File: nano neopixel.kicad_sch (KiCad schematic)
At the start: 12 parts

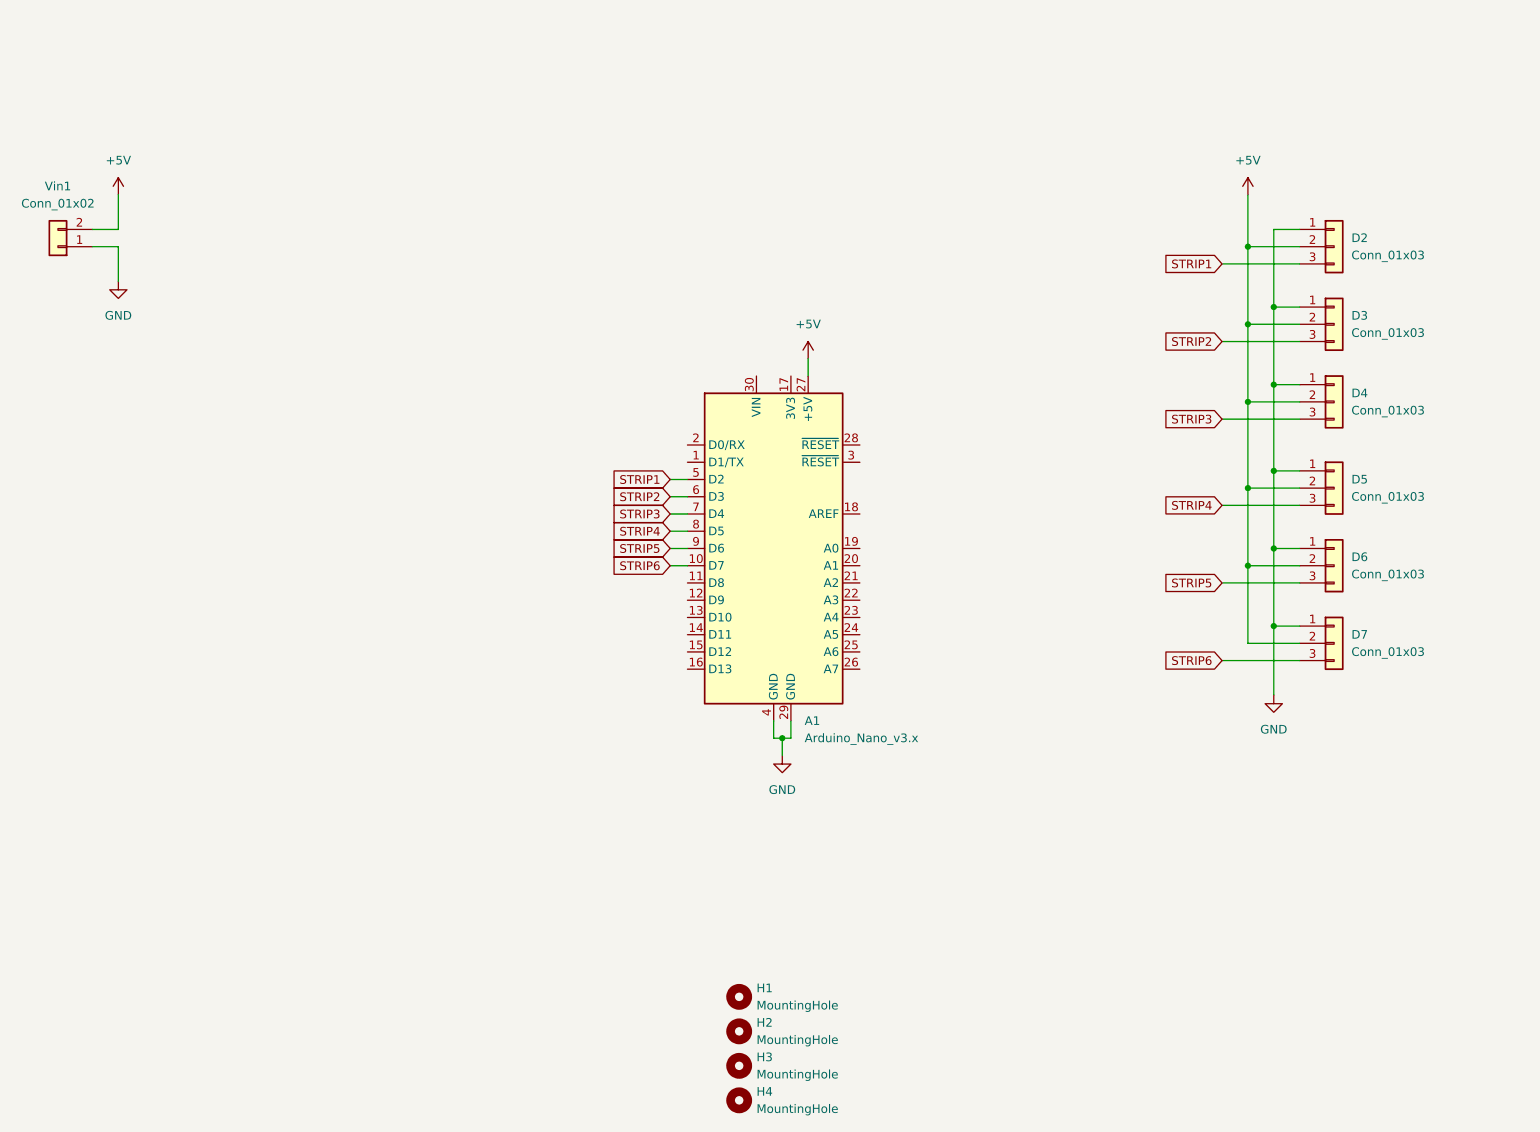
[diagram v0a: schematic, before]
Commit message: added 470ohm signal series resistors, and 1000uF tank cap on Vin
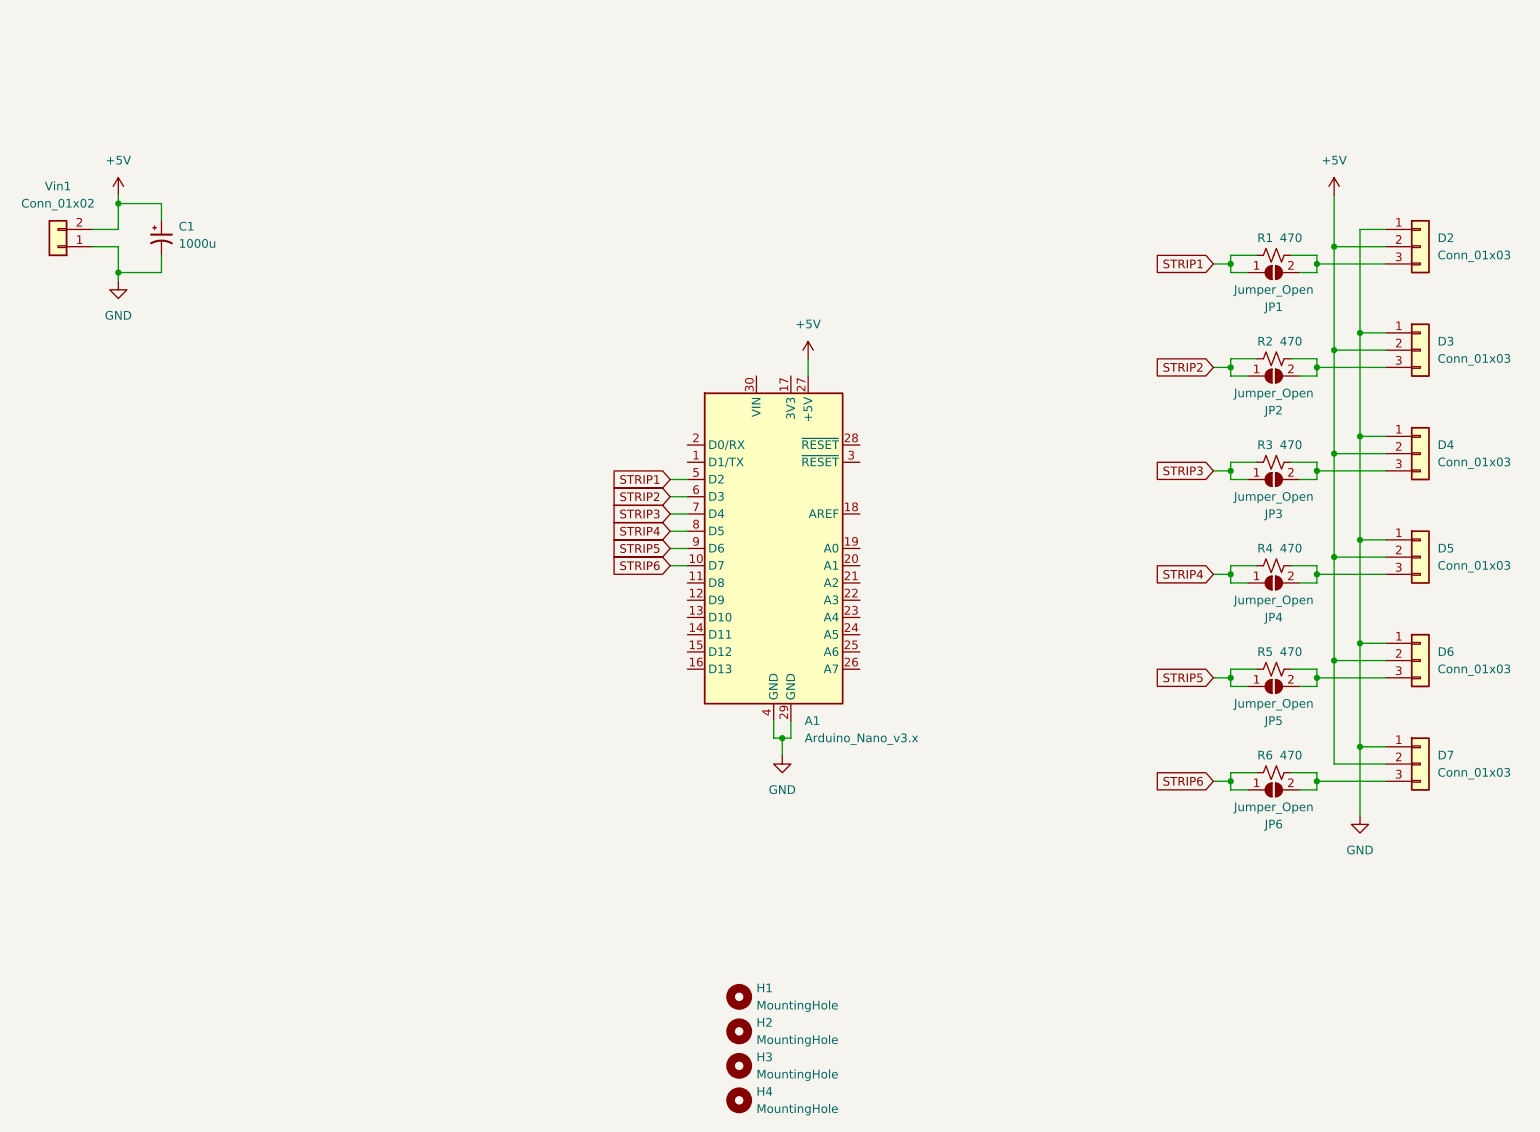
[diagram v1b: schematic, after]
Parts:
- added C1: 1000u, symbol Device:C_Polarized_Small_US
- added JP1, JP2, JP3, JP4, JP5, JP6: Jumper_Open, Jumper:SolderJumper-2_P1.3mm_Open_Pad1.0x1.5mm, symbol Jumper:SolderJumper_2_Open
- added R1, R2, R3, R4, R5, R6: 470, Resistor_SMD:R_0805_2012Metric, symbol Device:R_Small_US
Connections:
- net +5V: now also C1.1
- net GND: now also C1.2
- net STRIP1: now also JP1.1 (A), R1.1; no longer D2.3 (Pin_3)
- net STRIP2: now also JP2.1 (A), R2.1; no longer D3.3 (Pin_3)
- net STRIP3: now also JP3.1 (A), R3.1; no longer D4.3 (Pin_3)
- net STRIP4: now also JP4.1 (A), R4.1; no longer D5.3 (Pin_3)
- net STRIP5: now also JP5.1 (A), R5.1; no longer D6.3 (Pin_3)
- net STRIP6: now also JP6.1 (A), R6.1; no longer D7.3 (Pin_3)
- new net: D3.3 (Pin_3), JP2.2 (B), R2.2
- new net: D6.3 (Pin_3), JP5.2 (B), R5.2
- new net: D5.3 (Pin_3), JP4.2 (B), R4.2
- new net: D2.3 (Pin_3), JP1.2 (B), R1.2
- new net: D7.3 (Pin_3), JP6.2 (B), R6.2
- new net: D4.3 (Pin_3), JP3.2 (B), R3.2
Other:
- moved on the sheet: D2, D3, D4, D5, D6, D7

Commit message: added 2 more DIO connections, routed all traces
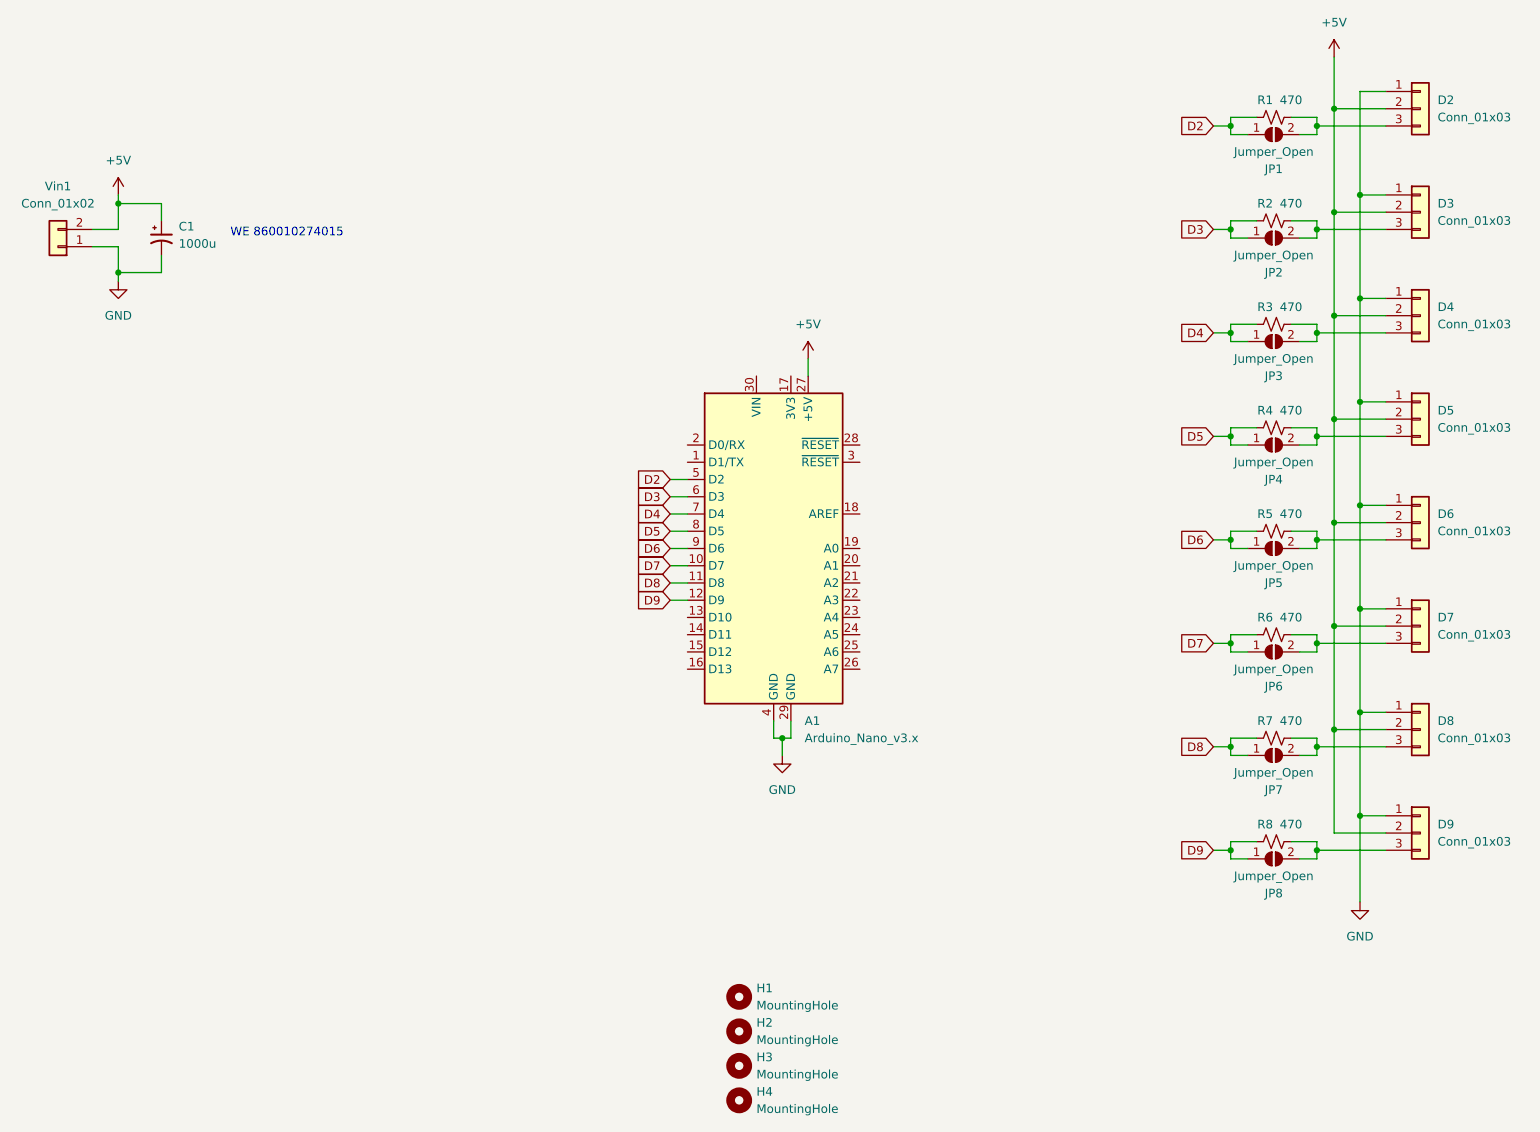
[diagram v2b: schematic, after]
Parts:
- added D8, D9: Conn_01x03, Connector_PinHeader_2.54mm:PinHeader_1x03_P2.54mm_Vertical, symbol Connector_Generic:Conn_01x03
- added JP7, JP8: Jumper_Open, Jumper:SolderJumper-2_P1.3mm_Open_Pad1.0x1.5mm, symbol Jumper:SolderJumper_2_Open
- added R7, R8: 470, Resistor_SMD:R_0805_2012Metric, symbol Device:R_Small_US
- C1: footprint (none) -> Capacitor_THT:CP_Radial_D8.0mm_P3.50mm
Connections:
- net +5V: now also D8.2 (Pin_2), D9.2 (Pin_2)
- net GND: now also D8.1 (Pin_1), D9.1 (Pin_1)
- net D8: now reaches A1.11 (D8)
- net D8: now also JP7.1 (A), R7.1
- net D9: now reaches A1.12 (D9)
- net D9: now also JP8.1 (A), R8.1
- net STRIP1 renamed D2
- net STRIP2 renamed D3
- net STRIP3 renamed D4
- net STRIP4 renamed D5
- net STRIP5 renamed D6
- net STRIP6 renamed D7
- new net: D8.3 (Pin_3), JP7.2 (B), R7.2
- new net: D9.3 (Pin_3), JP8.2 (B), R8.2
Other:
- note added: "WE 860010274015"
- moved on the sheet: D2, D3, D4, D5, D6, D7, JP1, JP2, JP3, JP4, JP5, JP6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

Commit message: added DIO labels to the resistors and jumpers
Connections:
- no-connect marks 0 -> 19
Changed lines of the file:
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@@
   (junction (at 224.79 36.83) (diameter 0) (color 0 0 0 0)
   )
+  (no_connect (at 157.48 99.06))
+  (no_connect (at 157.48 101.6))
+  (no_connect (at 157.48 104.14))
+  (no_connect (at 157.48 106.68))
+  (no_connect (at 157.48 109.22))
+  (no_connect (at 132.08 109.22))
+  (no_connect (at 132.08 111.76))
+  (no_connect (at 132.08 114.3))
+  (no_connect (at 132.08 86.36))
+  (no_connect (at 132.08 83.82))
+  (no_connect (at 142.24 73.66))
+  (no_connect (at 147.32 73.66))
+  (no_connect (at 157.48 83.82))
+  (no_connect (at 157.48 86.36))
+  (no_connect (at 157.48 93.98))
+  (no_connect (at 157.48 111.76))
+  (no_connect (at 157.48 114.3))
+  (no_connect (at 157.48 116.84))
+  (no_connect (at 132.08 116.84))
   (wire (pts (xy 212.09 96.52) (xy 212.09 97.79))
     (stroke (width 0) (type default) (color 0 0 0 0))

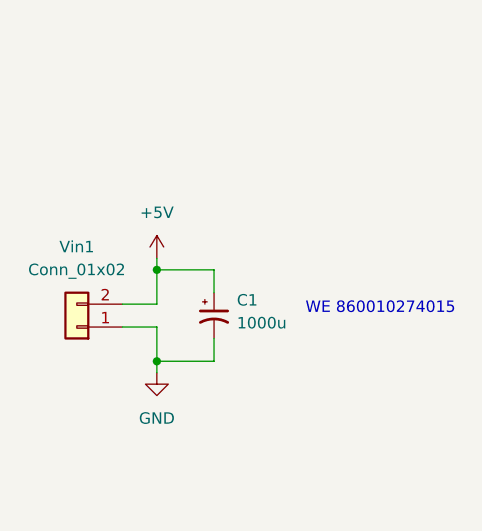
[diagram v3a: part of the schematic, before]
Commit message: Added JLC tracking number location
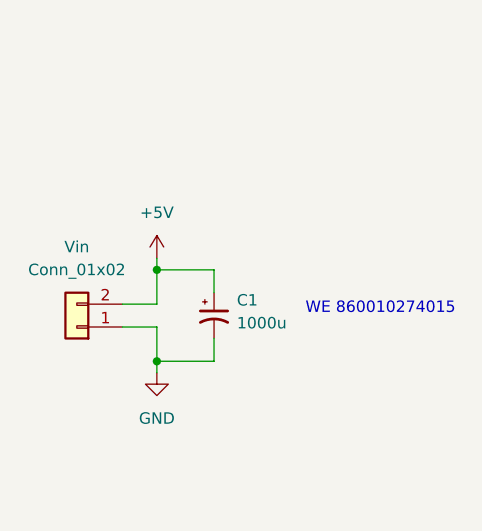
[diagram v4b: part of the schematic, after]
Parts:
- renumbered Vin1 to Vin
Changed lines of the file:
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@@
   (symbol (lib_id "Connector_Generic:Conn_01x02") (at 39.37 54.61 180) (unit 1)
     (in_bom yes) (on_board yes) (fields_autoplaced)
-    (property "Reference" "Vin1" (id 0) (at 39.37 45.72 0))
+    (property "Reference" "Vin" (id 0) (at 39.37 45.72 0))
     (property "Value" "Conn_01x02" (id 1) (at 39.37 48.26 0))
     (property "Footprint" "Connector_PinHeader_2.54mm:PinHeader_1x02_P2.54mm_Vertical" (id 2) (at 39.37 54.61 0)
@@
     )
     (path "/555fd684-9a58-4921-bd99-3bf42d5279c2"
-      (reference "Vin1") (unit 1) (value "Conn_01x02") (footprint "Connector_PinHeader_2.54mm:PinHeader_1x02_P2.54mm_Vertical")
-    )
-  )
+      (reference "Vin") (unit 1) (value "Conn_01x02") (footprint "Connector_PinHeader_2.54mm:PinHeader_1x02_P2.54mm_Vertical")
+    )
+  )

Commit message: added revision
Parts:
- C1: Manufactuter (none) -> Würth Elektronik; mfn (none) -> 860010274015
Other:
- note removed: "WE 860010274015"
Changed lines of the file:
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@@
 (kicad_sch (version 20211123) (generator eeschema)
   (paper "A4")
+  (title_block
+    (date "3/17/2022")
+    (rev "1.1")
+  )
   (junction (at 227.33 80.01) (diameter 0) (color 0 0 0 0)
   )
@@
   (wire (pts (xy 220.98 81.28) (xy 224.79 81.28))
     (stroke (width 0) (type default) (color 0 0 0 0))
-  )
-  (text "WE 860010274015" (at 64.77 53.34 0)
-    (effects (font (size 1.27 1.27)) (justify left bottom))
   )
   (global_label "D2" (shape input) (at 209.55 36.83 180) (fields_autoplaced)
@@
   )
   (symbol (lib_id "Device:C_Polarized_Small_US") (at 54.61 53.34 0) (unit 1)
-    (in_bom yes) (on_board yes) (fields_autoplaced)
+    (in_bom yes) (on_board yes)
     (property "Reference" "C1" (id 0) (at 57.15 51.6381 0)
       (effects (font (size 1.27 1.27)) (justify left))
@@
       (effects (font (size 1.27 1.27)) hide)
     )
-    (property "Datasheet" "~" (id 3) (at 54.61 53.34 0)
-      (effects (font (size 1.27 1.27)) hide)
-    )
-    (pin "1")
+    (property "Datasheet" "https://www.we-online.com/katalog/datasheet/860010274015.pdf" (id 3) (at 54.61 53.34 0)
+      (effects (font (size 1.27 1.27)) hide)
+    )
+    (property "mfn" "860010274015" (id 4) (at 57.15 59.69 0)
+      (effects (font (size 1.27 1.27)) (justify left))
+    )
+    (property "Manufactuter" "Würth Elektronik" (id 5) (at 57.15 57.15 0)
+      (effects (font (size 1.27 1.27)) (justify left))
+    )
+    (pin "1")

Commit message: updated title block with 4488 info
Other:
- company: (none) -> FRC 4488 - SHOCKWAVE
- title: (none) -> NeoPixel driver
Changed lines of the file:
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@@
   (paper "A4")
   (title_block
+    (title "NeoPixel driver")
     (date "3/17/2022")
-    (rev "1.1")
+    (rev "1.0")
+    (company "FRC 4488 - SHOCKWAVE")
   )
   (junction (at 227.33 80.01) (diameter 0) (color 0 0 0 0)
